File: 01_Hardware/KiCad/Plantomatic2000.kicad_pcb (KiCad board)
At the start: 4 copper layers, 84.5 x 50.4 mm, 207 parts, among them J101 Conn_02x05_Odd_Even, J102 Conn_02x03_Odd_Even, J103 USB_C_Receptacle_USB2.0_16P, J105 JST_B4B, J106 Line Select, J107 Manual Start, J108 Hour, J109 Minute, J110 JST_4B4, J111 System Reset, J112 JST_B2B, J113 JST_B2B, J114 System Wake Up, J115 Running LED, J116 JST_4B4, J117 Running LED, Q101 IRLL014NP, Q102 IRLL014NP, Q104 NVTA7002NT1G, Q105 RU1E002SPTCL, Q106 NVTA7002NT1G, Q107 NVTA7002NT1G, Q108 RU1E002SPTCL, Q109 NVTA7002NT1G, Q110 RU1E002SPTCL, Q111 DTC143Z, Q112 DTC143Z, Q113 CSD17313Q2, SW102 SW_Push, SW103 SW_Push, U101 XC6220B331MR, U102 nPM1300, U103 ESP32-WROOM-32E, U104 TPS61287, U105 USBLC6-2P6, U106 CP2102N-A02-GQFN24, U107 DS3231M, U108 AT24CS01-SSHM

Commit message: Finished PCB design
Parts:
- removed TP114, TP119, TP124, TP128, TP129: ~, TestPoint:TestPoint_Pad_D1.0mm
- C115, J102, TP120: moved to F.Cu
- moved C116 57.3 mm to (134.2, 113.9), turned to 180 degrees
- moved J101 46.5 mm to (132.1, 109.0), turned to 90 degrees
- moved BT101 38.9 mm to (147.2, 120.4), turned to 45 degrees
- moved C115 29.4 mm to (164.9, 80.3)
- moved D106 23.4 mm to (141.2, 86.2)
- moved R122 22.1 mm to (139.9, 83.2), turned to 90 degrees
- moved J102 21.8 mm to (169.8, 79.5), turned to 180 degrees
- moved H103 15.0 mm to (126.6, 122.9)
- moved H105 6.78 mm to (189.6, 116.9)
- moved TP120 5.73 mm to (168.8, 95.0), turned to 0 degrees
- moved R153 5.38 mm to (154.1, 88.6), turned to -90 degrees
- moved TP118 5.04 mm to (159.3, 82.0)
- moved TP117 4.87 mm to (161.6, 83.8)
- moved C144 3.98 mm to (147.4, 91.0), turned to -90 degrees
- moved R152 3.35 mm to (155.9, 88.6), turned to -90 degrees
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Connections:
- J103 pad S1: unconnected-(J103-SHIELD-PadS1)_3 -> GND
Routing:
- net +3V3: track 33.3 -> 160.3 mm, vias 8 -> 18
- net VBUS: track 16.3 -> 135.3 mm, vias 0 -> 6
- net Net-(BT101-+): track 2.89 -> 83.6 mm, vias 0 -> 1
- net WATER_SENSOR_SIG: track 0.00 -> 74.2 mm, vias 0 -> 1
- net WATER_SENSOR_EN: track 0.78 -> 73.9 mm, vias 0 -> 2
- net PMIC_SHPHLD: track 2.51 -> 72.4 mm, vias 1 -> 4
- net /ESP_EN: track 6.69 -> 70.2 mm, vias 0 -> 4
- net Net-(J116-Pin_1): track 0.68 -> 56.5 mm, vias 1 -> 2
- net /ESP_IO0: track 4.22 -> 54.6 mm, vias 0 -> 4
- net +VSYS: track 36.7 -> 85.9 mm
- net PUMP1_EN: track 0.89 -> 44.5 mm
- net Net-(J116-Pin_2): track 0.68 -> 41.9 mm
- net DISPLAY_ENABLE: track 0.78 -> 37.3 mm, vias 0 -> 2
- net Net-(J116-Pin_3): track 0.68 -> 36.7 mm, vias 1 -> 0
- net /ESP_TDO: track 0.00 -> 31.9 mm, vias 0 -> 1
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- added copper zone on In1.Cu, net +12V
- added copper zone on In1.Cu, net VBUS
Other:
- board size 84.5 x 50.4 mm -> 84 x 51 mm

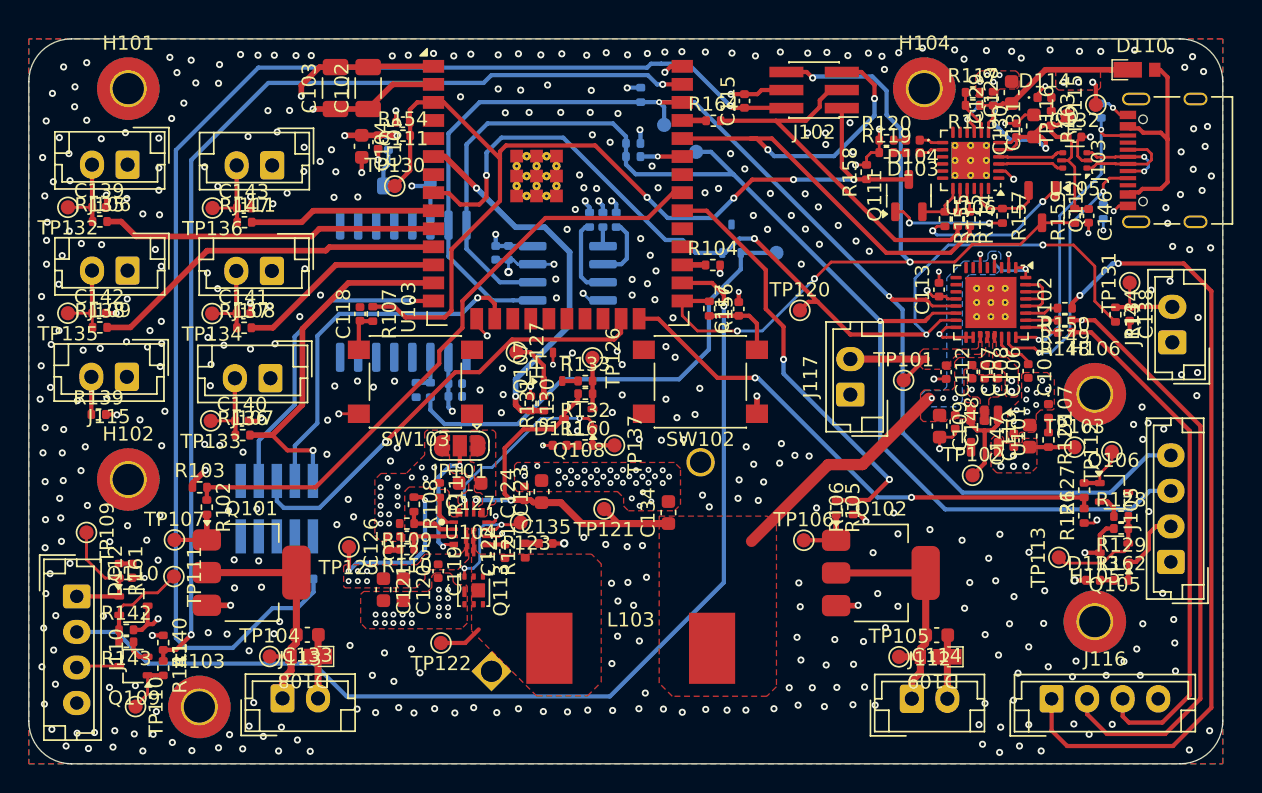
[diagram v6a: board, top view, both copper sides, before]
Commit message: Finished PCB design / Added Mounting holes position / Plantomatic2000.step generated / Gerber files generated
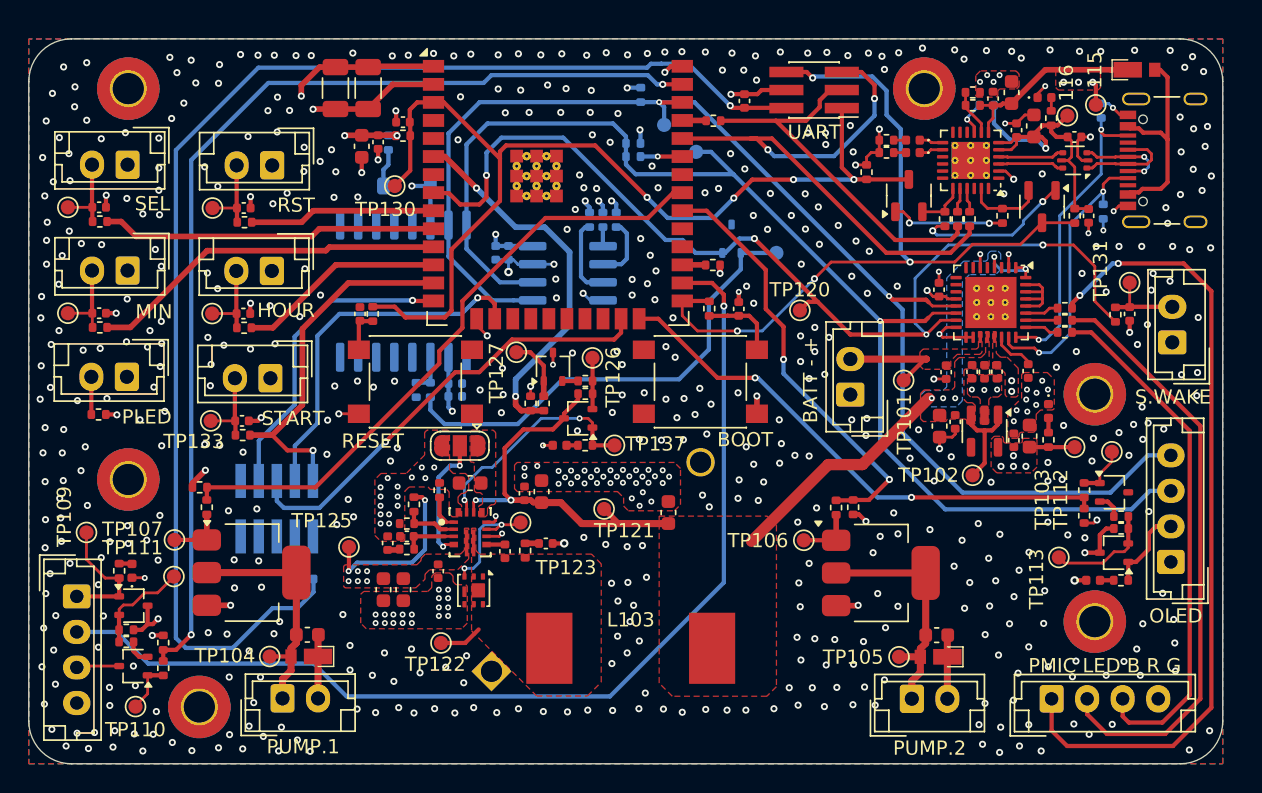
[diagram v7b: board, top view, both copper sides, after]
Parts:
- BATT - +: renamed from J117
- PMIC LED B R G: renamed from J116
- Water Sig: renamed from J110
- renumbered TP115 to 115, TP116 to 116, TP132 to 132, TP136 to 136, SW102 to BOOT, J108 to HOUR, J101 to JTAG, J109 to MIN, J105 to OLED, J115 to PLED, J113 to PUMP.1, J112 to PUMP.2, SW103 to RESET, J111 to RST, J114 to S.WAKE, JP101 to SEL, J106 to SEL, J107 to START, J102 to UART
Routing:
- net Net-(J116-Pin_2): vias 1 -> 0
- net GND: vias 551 -> 633
- added copper zone on In1.Cu, net +3V3
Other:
- board text added: "Plantomatic2000 v0.1 20250625"
